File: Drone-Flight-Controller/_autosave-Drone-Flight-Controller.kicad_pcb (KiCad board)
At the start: 2 copper layers, 30 x 65 mm, 66 parts, among them J1 TestPoint, J10 TestPoint, J11 TestPoint, J12 TestPoint, J13 TestPoint, J2 TestPoint, J3 2044-2X20G00RA, J4 TestPoint, J5 TestPoint, J6 TestPoint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

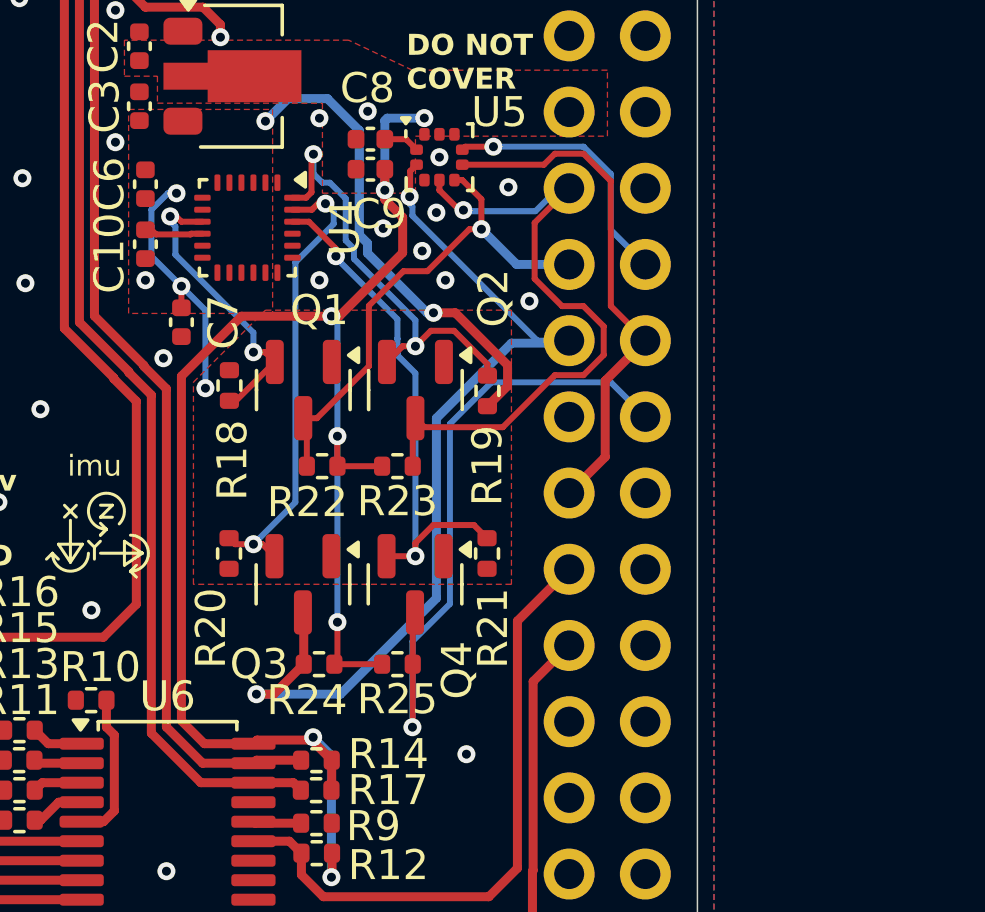
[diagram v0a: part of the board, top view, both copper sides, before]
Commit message: level shifters are a single part now
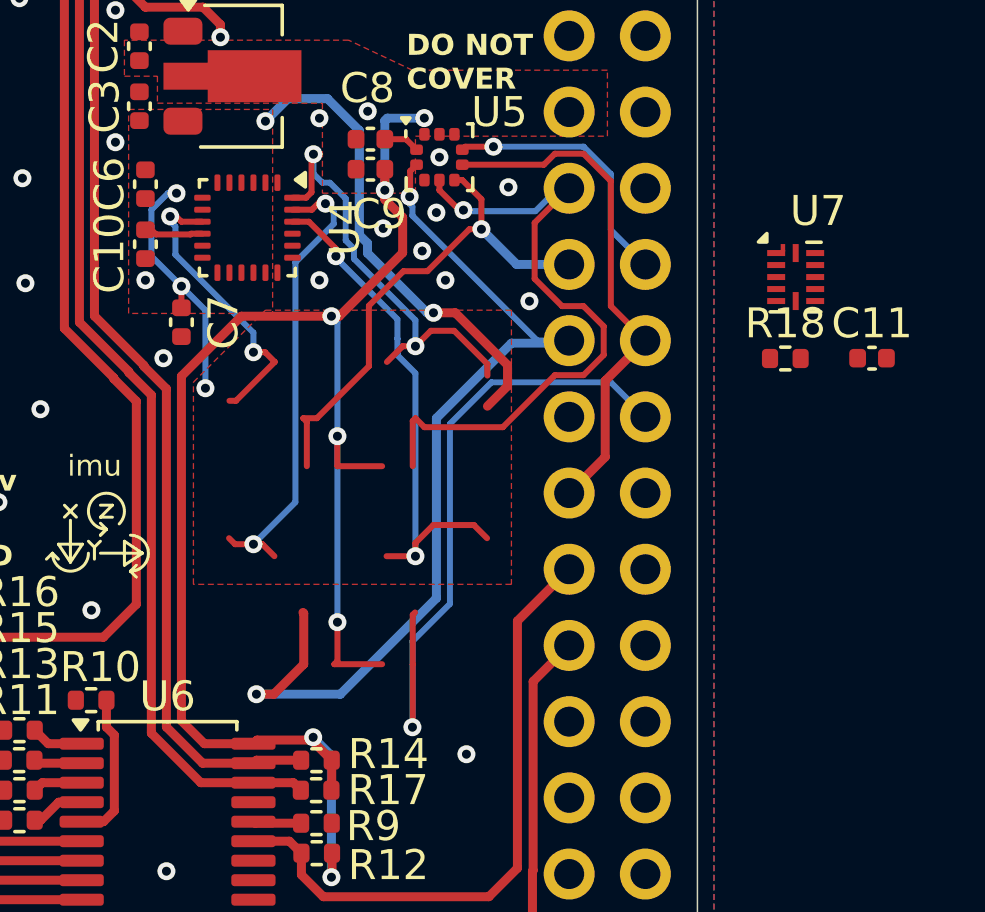
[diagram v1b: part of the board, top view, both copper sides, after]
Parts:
- removed Q1, Q2, Q3, Q4: BSS138, Package_TO_SOT_SMD:SOT-23
- removed R19, R20, R21, R22, R23, R24, R25: RK73G1ERTTP1002F, Resistor_SMD:R_0402_1005Metric
- added C11: C1005X5R1C104K050BA, Capacitor_SMD:C_0402_1005Metric, F.Cu at (48.0, 49.0)
- added U7: TXBN0304RUT, Package_DFN_QFN:Texas_R-PUQFN-N12, F.Cu at (45.5, 46.3)
- moved R18 18.6 mm to (45.1, 49.0), turned to 0 degrees
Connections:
- R18 pad 1: SPI0_SDO_LV -> Net-(U7-~{OE})
- R18 pad 2: +1V8 -> GND
